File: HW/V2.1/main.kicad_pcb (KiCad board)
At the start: 2 copper layers, 100 x 100 mm, 177 parts, among them IC1 RT9466, IC2 MIC4416, IC3 MIC4416, J4 USB-C, Q1 FDN360P, Q2 NTMS4816NR2G, Q3 NTMS4816NR2G, Q4 FDN360P, T1 TS-1136EVW, T2 TS-1136EVW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

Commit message: updated values
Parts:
- removed F1: 120R@100MHz, Resistor_SMD:R_0805_2012Metric
- removed G***: LOGO, otter:EO_TOUCH
- removed G***: LOGO, otter:EO_OTTTER
- removed G***: LOGO, otter:EO_TEXT
- removed G***: LOGO, otter:EO_PLUS
- removed G***: LOGO, otter:EO_MINUS
- removed G1: LOGO, otter:power_0707
- removed G_BRIGHTNESS_1: LOGO, otter:brightness_0707
- removed G_COLORPICKER_1: LOGO, otter:color_picker_0707
- added FB2: Ferret, Inductor_SMD:L_0805_2012Metric, B.Cu at (93.5, 101.4)
- C11, C15: value 4u7 16V -> 82n
- C23: value 4.7u 25V -> 10u 25V
- C8: value 10u 6,3V -> 1u 25V
- C9: value 22p 50V -> 18p 50V
- FB1: value Ferrite_Bead -> Ferret
- NTC1: value 10k -> DNP
- R32: value 47k -> 220k
- R33: value 4k7 -> 47k
- R35, R38: value 22 -> 5
- T1, T2: value TS-1136EVW -> Panasonic_EVQPUL_EVQPUC
- U1: value STM32F302-SQ48 -> STM32F334

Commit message: fixed opamp
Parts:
- U4: value LM358 -> MCP6L2T-E/MS
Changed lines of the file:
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@@
       (effects (font (size 0.45 0.45) (thickness 0.1)) (justify mirror))
     )
-    (fp_text value LM358 (at 0 -2.6 180) (layer B.Fab)
+    (fp_text value MCP6L2T-E/MS (at 0 -2.6 180) (layer B.Fab)
       (effects (font (size 1 1) (thickness 0.15)) (justify mirror))
     )

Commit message: fixed voltage divider for current measurement
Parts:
- R48, R49: value 10k -> 12k
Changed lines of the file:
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@@
       (effects (font (size 0.45 0.45) (thickness 0.1)) (justify mirror))
     )
-    (fp_text value 10k (at 0 -1.43) (layer B.Fab)
+    (fp_text value 12k (at 0 -1.43) (layer B.Fab)
       (effects (font (size 1 1) (thickness 0.15)) (justify mirror))
     )
@@
       (effects (font (size 0.45 0.45) (thickness 0.1)) (justify mirror))
     )
-    (fp_text value 10k (at 0 -1.43 270) (layer B.Fab)
+    (fp_text value 12k (at 0 -1.43 270) (layer B.Fab)
       (effects (font (size 1 1) (thickness 0.15)) (justify mirror))
     )

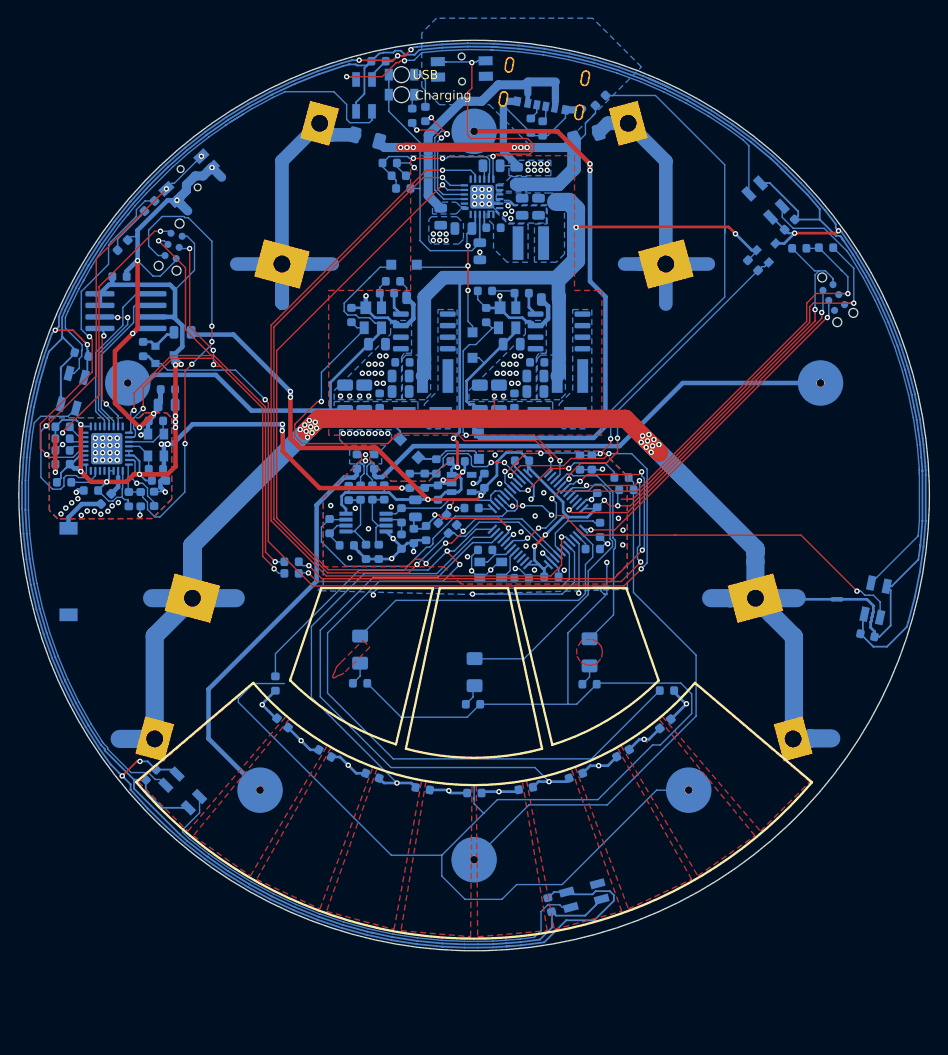
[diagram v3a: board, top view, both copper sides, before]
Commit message: added touch ic, fixed sk6812
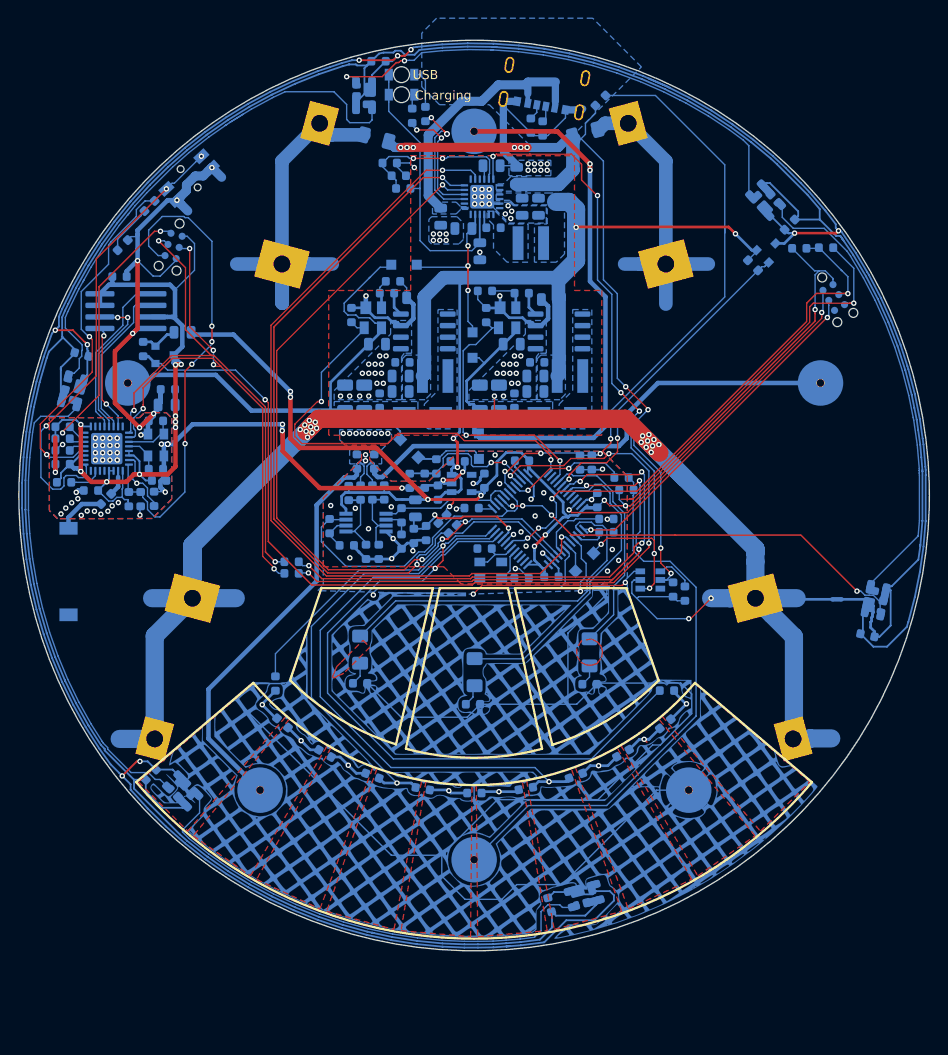
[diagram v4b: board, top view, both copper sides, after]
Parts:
- removed T1: Panasonic_EVQPUL_EVQPUC, Button_Switch_SMD:Panasonic_EVQPUL_EVQPUC
- added C46: 18p 50V, Capacitor_SMD:C_0603_1608Metric, B.Cu at (123.2, 110.8)
- added C58: 100n 50V, Capacitor_SMD:C_0603_1608Metric, B.Cu at (121.8, 110.3)
- added D10: D, Diode_SMD:D_SOD-123F, B.Cu at (112.1, 107.3)
- added G***: LOGO, otter:EO_TOUCH, F.Cu at (101.1, 129.4)
- added U6: BS801B, Package_TO_SOT_SMD:SOT-23-6, B.Cu at (119.3, 109.3)
- LED1, LED2, LED3, LED4, LED5, LED9: footprint LED_SMD:LED_SK6812MINI_PLCC4_3.5x3.5mm_P1.75mm -> otter:sk6812mini
- moved C15 2.38 mm to (114.5, 104.0)
- moved R18 1.39 mm to (114.5, 102.6), turned to 0 degrees
- moved R34 1.02 mm to (89.2, 60.8)
- moved R31 0.35 mm to (112.2, 60.1)
- moved C12 0.16 mm to (101.2, 105.8)
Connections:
- IC1 pad 12: Net-(IC1-Pad12) -> TOUCH_POWER
- U1 pad 42: TOUCH7 -> Net-(D10-Pad2)
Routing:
- net TOUCH_POWER: track 0.00 -> 73.7 mm, vias 0 -> 7
- net VBAT+: track 40.2 -> 96.2 mm, vias 6 -> 10
- net Net-(IC1-Pad12): track 29.1 -> 0.00 mm, vias 2 -> 0
- net GND: track 604.5 -> 612.0 mm, vias 167 -> 163
- net LED3: track 34.3 -> 39.5 mm
- net Net-(C46-Pad2): track 0.00 -> 4.19 mm
- net TOUCH7: track 16.1 -> 19.5 mm, vias 1 -> 2
- net Net-(D10-Pad2): track 0.00 -> 3.20 mm
- net TOUCH2: track 100.9 -> 98.8 mm
- net NTC: track 60.2 -> 61.9 mm
- net KathodeW: track 58.0 -> 59.5 mm
- net TOUCH5: track 1.84 -> 3.29 mm
- net Net-(254_2-Pad+): track 39.0 -> 40.0 mm
- net LED1: track 24.7 -> 25.5 mm
- net OTG: track 90.9 -> 90.1 mm
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
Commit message: routed board
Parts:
- removed G***: LOGO, otter:EO_TOUCH
- moved C58 4.15 mm to (119.3, 107.0), turned to 180 degrees
- moved C46 1.82 mm to (121.8, 109.5)
- moved NT1 0.32 mm to (140.1, 111.7), turned to 135 degrees
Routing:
- net TOUCH2: track 98.8 -> 102.4 mm
- net GND: track 612.0 -> 609.2 mm, vias 163 -> 167
- net Net-(C46-Pad2): track 4.19 -> 1.53 mm
- net Net-(LED3-Pad3): track 54.2 -> 52.1 mm
- net VSYS_SK6812: track 318.3 -> 320.3 mm
- net Net-(LED2-Pad3): track 58.4 -> 57.1 mm
- net TOUCH_POWER: track 73.7 -> 73.1 mm
- net SK6812: track 48.0 -> 48.6 mm
- net GNDD: track 314.2 -> 314.1 mm, vias 0 -> 2

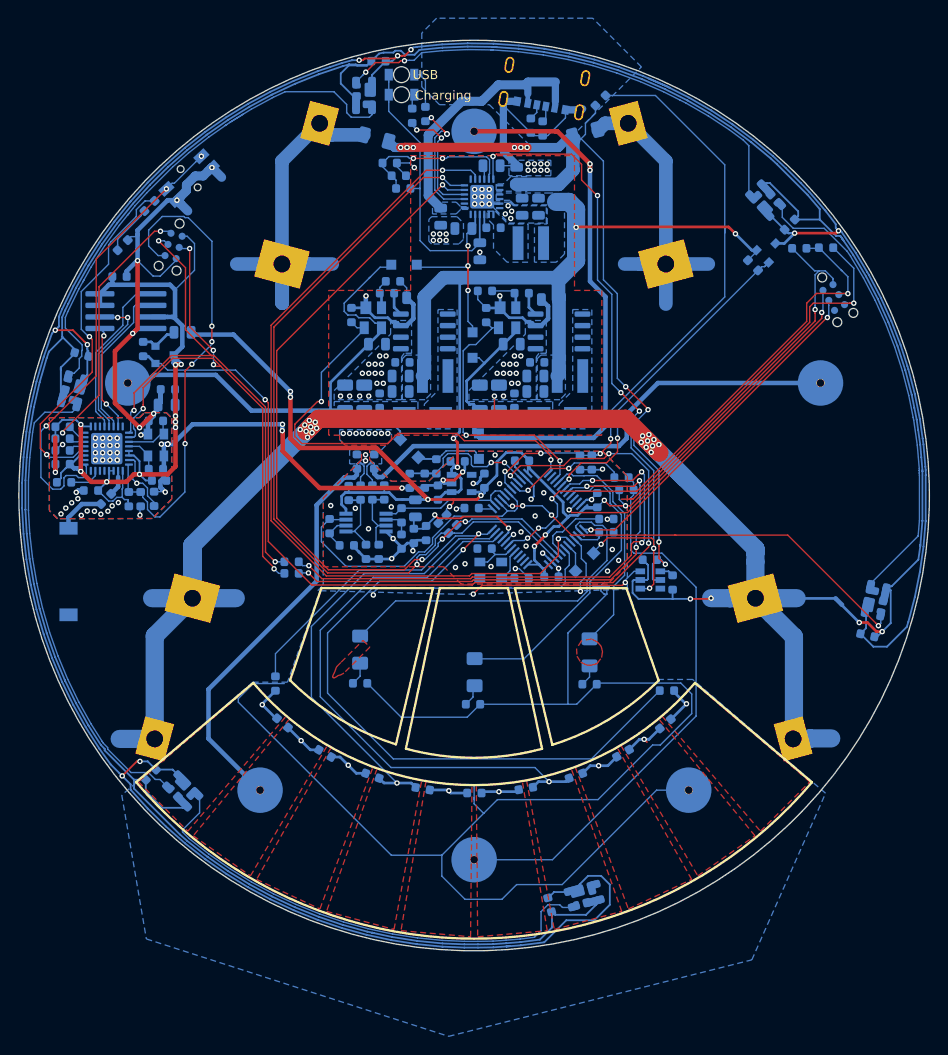
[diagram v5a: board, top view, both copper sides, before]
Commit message: enlarged pads
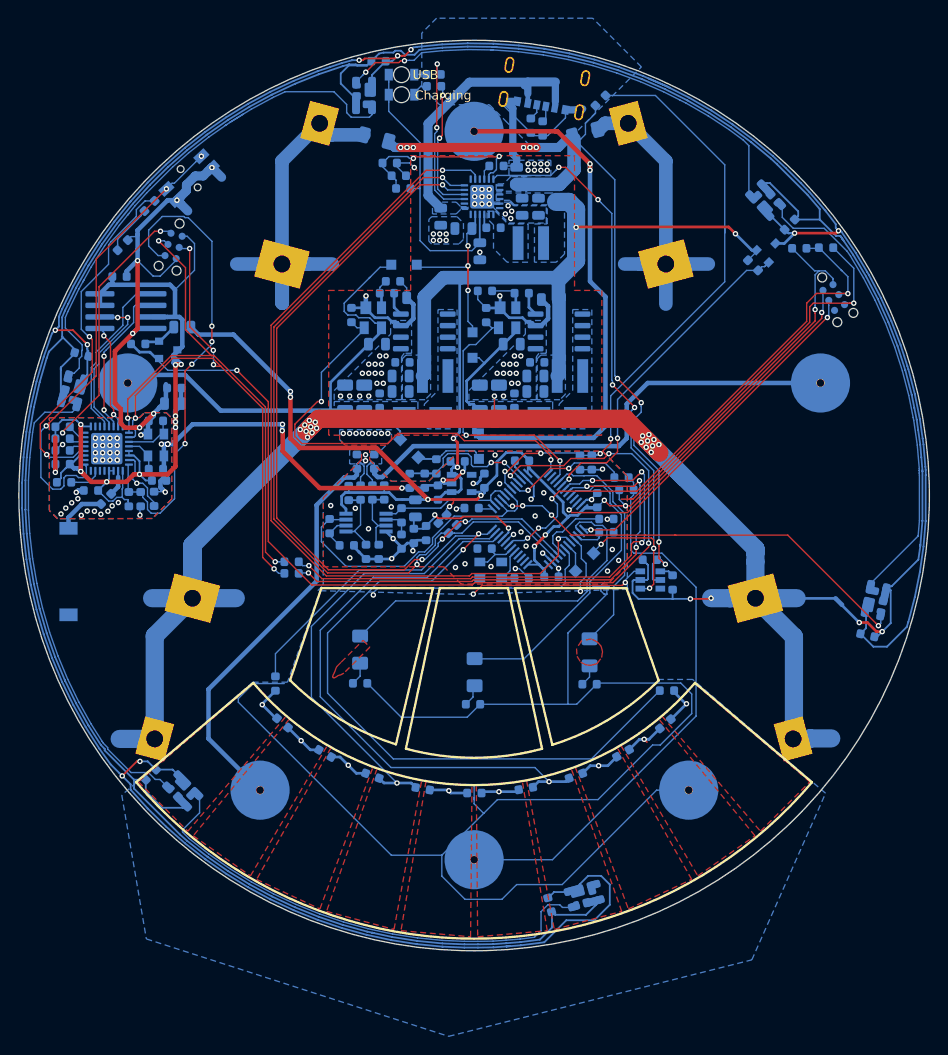
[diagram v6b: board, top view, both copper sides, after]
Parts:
- R29: footprint Resistor_SMD:R_0805_2012Metric -> Resistor_SMD:R_0603_1608Metric
- moved R28 4.44 mm to (95.5, 53.8), turned to 0 degrees
- moved R27 4.03 mm to (95.6, 55.0), turned to 180 degrees
- moved R17 0.79 mm to (63.1, 83.3), turned to 0 degrees
- moved C14 0.72 mm to (66.9, 89.9)
- moved C13 0.72 mm to (67.1, 88.2)
- moved Q1 0.68 mm to (66.4, 84.0)
- moved FB1 0.58 mm to (68.0, 81.5)
- moved R29 0.54 mm to (102.5, 63.8)
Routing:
- net TOUCH_POWER: track 73.1 -> 68.7 mm
- net Net-(IC1-Pad3): track 14.9 -> 18.9 mm, vias 3 -> 2
- net Net-(D8-Pad1): track 4.40 -> 1.35 mm
- net NTCBAT: track 17.9 -> 19.8 mm
- net ESP: track 103.1 -> 105.0 mm
- net Net-(IC1-Pad4): track 13.0 -> 14.9 mm
- net SCL: track 85.3 -> 86.7 mm
- net VBAT+: track 96.2 -> 95.1 mm
- net VBUS: track 30.7 -> 31.5 mm
- net SK6812_EN: track 36.1 -> 36.9 mm
- net 3V3ESP: track 95.5 -> 94.8 mm
- net KathodeW: track 59.5 -> 60.1 mm
- net Net-(D7-Pad1): track 1.62 -> 2.21 mm
- net ESP_RST: track 53.6 -> 53.0 mm
- net ESP_SO: track 17.2 -> 17.0 mm, vias 0 -> 2

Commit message: drc done
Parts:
- added G***: LOGO, otter:brightness_0707, F.Cu at (112.7, 117.2)
- added G***: LOGO, otter:color_picker_0707, F.Cu at (87.5, 116.9)
- added G***: LOGO, otter:EO_OTTTER, F.Cu at (99.5, 83.7)
- added G***: LOGO, otter:EO_MINUS, F.Cu at (74.0, 131.1)
- added G***: LOGO, otter:EO_PLUS, F.Cu at (126.1, 131.1)
- added G***: LOGO, otter:EO_TEXT, F.Cu at (133.4, 106.5)
- added G1: LOGO, otter:power_0707, F.Cu at (100.0, 119.4)
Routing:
- net GND: track 609.3 -> 611.0 mm
- net TOUCH7: vias 2 -> 1

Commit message: exported gerber
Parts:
- added G***: LOGO, otter:EO_TOUCH_1, F.Cu at (102.0, 129.2)
- added G***: LOGO, otter:EO_TOUCH_2, F.Cu at (102.0, 129.2)
- 254_1, 254_2: value 254 -> Val**
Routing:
- net GNDD: track 314.1 -> 313.5 mm
